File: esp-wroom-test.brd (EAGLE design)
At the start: 30.4 x 32.5 mm, 26 parts, among them J4 Vertical Qwiic Connector, SW1 AMAZON_BUTTONB2010, SW2 AMAZON_BUTTONB2010, U8 NCP1117LPST50T3G

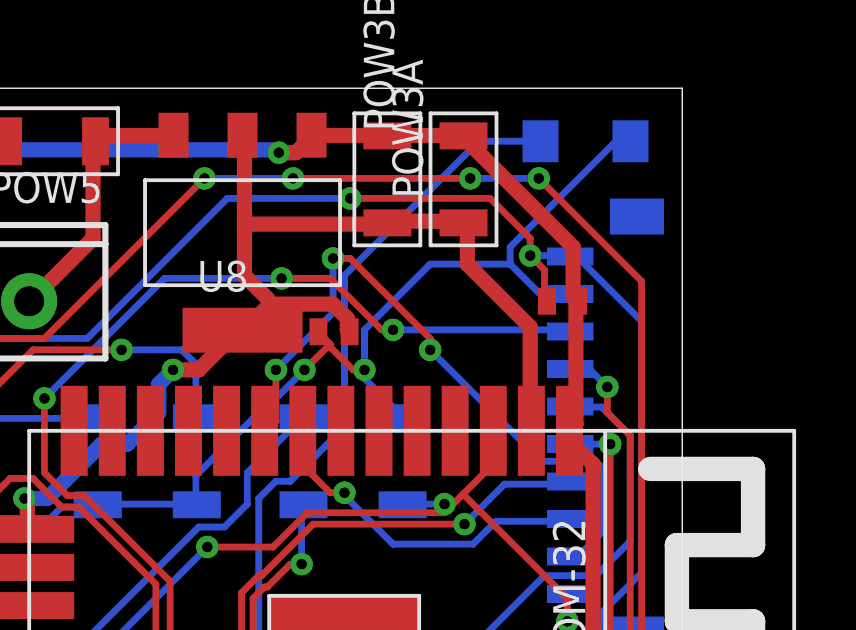
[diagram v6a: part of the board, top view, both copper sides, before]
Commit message: Add missing vcc gnd jumpers
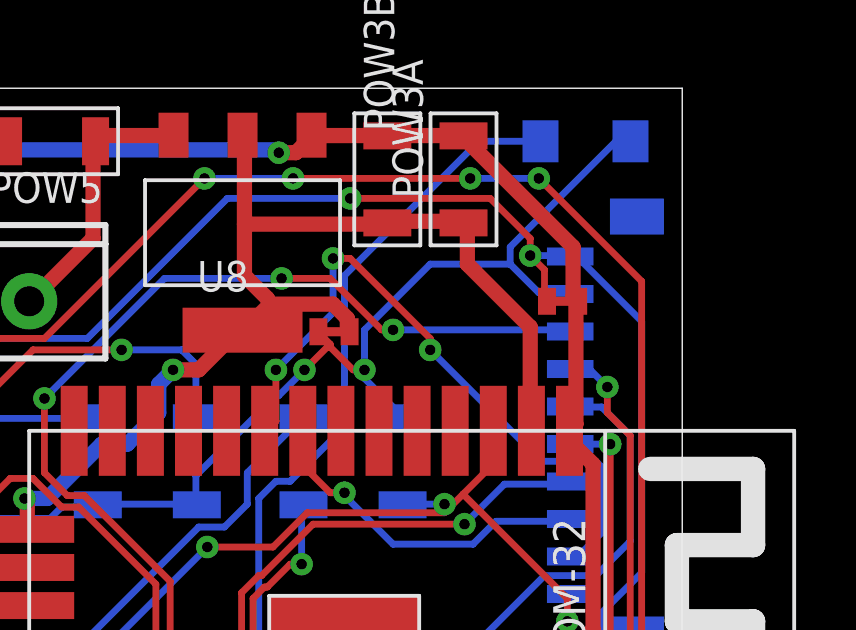
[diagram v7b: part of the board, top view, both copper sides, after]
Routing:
- net N$1: track 0.00 -> 1.02 mm
- net GND_HC: track 54.3 -> 55.3 mm
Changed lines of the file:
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@@
 <wire x1="26.8605" y1="21.05025" x2="26.8605" y2="25.146" width="0.508" layer="1"/>
 <wire x1="26.67" y1="20.85975" x2="26.8605" y2="21.05025" width="0.508" layer="1"/>
-<wire x1="26.8605" y1="25.146" x2="26.936" y2="25.146" width="0.508" layer="1"/>
+<wire x1="26.8605" y1="25.146" x2="26.924" y2="25.146" width="0.508" layer="1"/>
+<wire x1="26.924" y1="25.146" x2="26.936" y2="25.146" width="0.508" layer="1"/>
 <wire x1="26.67" y1="20.85975" x2="26.646" y2="20.828" width="0.508" layer="1"/>
 <wire x1="26.76525" y1="26.95575" x2="23.241" y2="30.48" width="0.508" layer="1"/>
@@
 <wire x1="17.907" y1="30.48" x2="18.048" y2="30.682" width="0.508" layer="1"/>
 <via x="16.9545" y="30.099" extent="1-16" drill="0.35"/>
+<wire x1="25.908" y1="25.146" x2="26.924" y2="25.146" width="0.3048" layer="1"/>
 </signal>
 <signal name="VCC_HC" class="3">
@@
 <via x="16.66875" y="7.71525" extent="1-16" drill="0.35"/>
 </signal>
+<signal name="N$1">
+<wire x1="18.288" y1="24.13" x2="19.304" y2="24.13" width="0.3048" layer="1"/>
+</signal>
 </signals>
